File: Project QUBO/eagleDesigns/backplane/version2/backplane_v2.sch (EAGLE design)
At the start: 5 parts

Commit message: 
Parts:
- added G10, G4, G5, G6, G7, G8, G9: (no value), avx:F930J107MBA
- added G2, G3: (no value), texas:TPS2044BBD-SOIC
- added U1: TUSB2077ALQFP, texas:TUSB2077ALQFP
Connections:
- new net !OVERCUR1!: G2.!OC1!
- new net !OVERCUR2!: G2.!OC2!
- new net !OVERCUR3!: G2.!OC3!
- new net !OVERCUR4!: G2.!OC4!
- new net !OVERCUR5!: G3.!OC1!
- new net !OVERCUR6!: G3.!OC2!
- new net !OVERCUR7!: G3.!OC3!
- new net !PWRON1!: G2.!EN1!
- new net !PWRON2!: G2.!EN2!
- new net !PWRON3!: G2.!EN3!
- new net !PWRON4!: G2.!EN4!
- new net !PWRON5!: G3.!EN1!
- new net !PWRON6!: G3.!EN2!
- new net !PWRON7!: G3.!EN3!
- new net N$1: U1.SUSPND
- new net N$11: U1.!PWRON1!
- new net N$12: U1.!OVERCUR1!
- new net N$13: U1.DM1
- new net N$14: U1.DP1
- new net N$15: U1.!PWRON2!
- new net N$16: U1.!OVERCUR2!
- new net N$17: U1.DM2
- new net N$18: U1.DP2
- new net N$19: U1.!PWRON3!
- new net N$2: U1.DP0PUR
- new net N$20: U1.!OVERCUR3!
- new net N$21: U1.DM3
- new net N$22: U1.DP3
- new net N$23: U1.!PWRON4!
- new net N$25: U1.!OVERCUR4!
- new net N$26: U1.DM4
- new net N$27: U1.DP4
- new net N$28: U1.!PWRON5!
- new net N$29: U1.!OVERCUR5!
- new net N$3: U1.DP0
- new net N$30: U1.DM5
- new net N$31: U1.DP5
- new net N$32: U1.!PWRON6!
- new net N$33: U1.!OVERCUR6!
- new net N$34: U1.DM6
- new net N$35: U1.DP6
- new net N$36: U1.!PWRON7!
- new net N$4: U1.DM0
- new net N$40: U1.XTAL1/CLK48
- new net N$41: U1.XTAL2
- new net N$43: U1.PORTDIS
- new net N$44: U1.PORTPWR
- new net N$45: U1.HUBCFG
- new net N$46: U1.DP7
- new net N$47: U1.DM7
- new net N$48: U1.!OVERCUR7!
- new net N$7: U1.EECLK
- new net USB-5V_2: G2.OUT2, JP2.P$63
- new net USB-5V_3: G2.OUT3, JP3.P$63
- new net USB-5V_4: G2.OUT4, JP4.P$63
- new net USB-5V_5: G3.OUT1
- new net USB-5V_6: G3.OUT2
- new net USB-5V_7: G3.OUT3
- net 3V3: now also U1.!BUSPWR!, U1.!EXTMEM!, U1.EEDATA/!GANGED!, U1.VCC@46, U1.VCC@9
- net 5V: now also G2.IN1, G2.IN2, G3.IN1, G3.IN2
- net GND: now also G2.GND1, G2.GND2, G3.GND1, G3.GND2, U1.GND@24, U1.GND@43, U1.GND@5, U1.MODE
- net GPIO_3: now also U1.!RESET!
- net USB-5V_1: now also G2.OUT1; no longer JP2.P$63, JP3.P$63, JP4.P$63

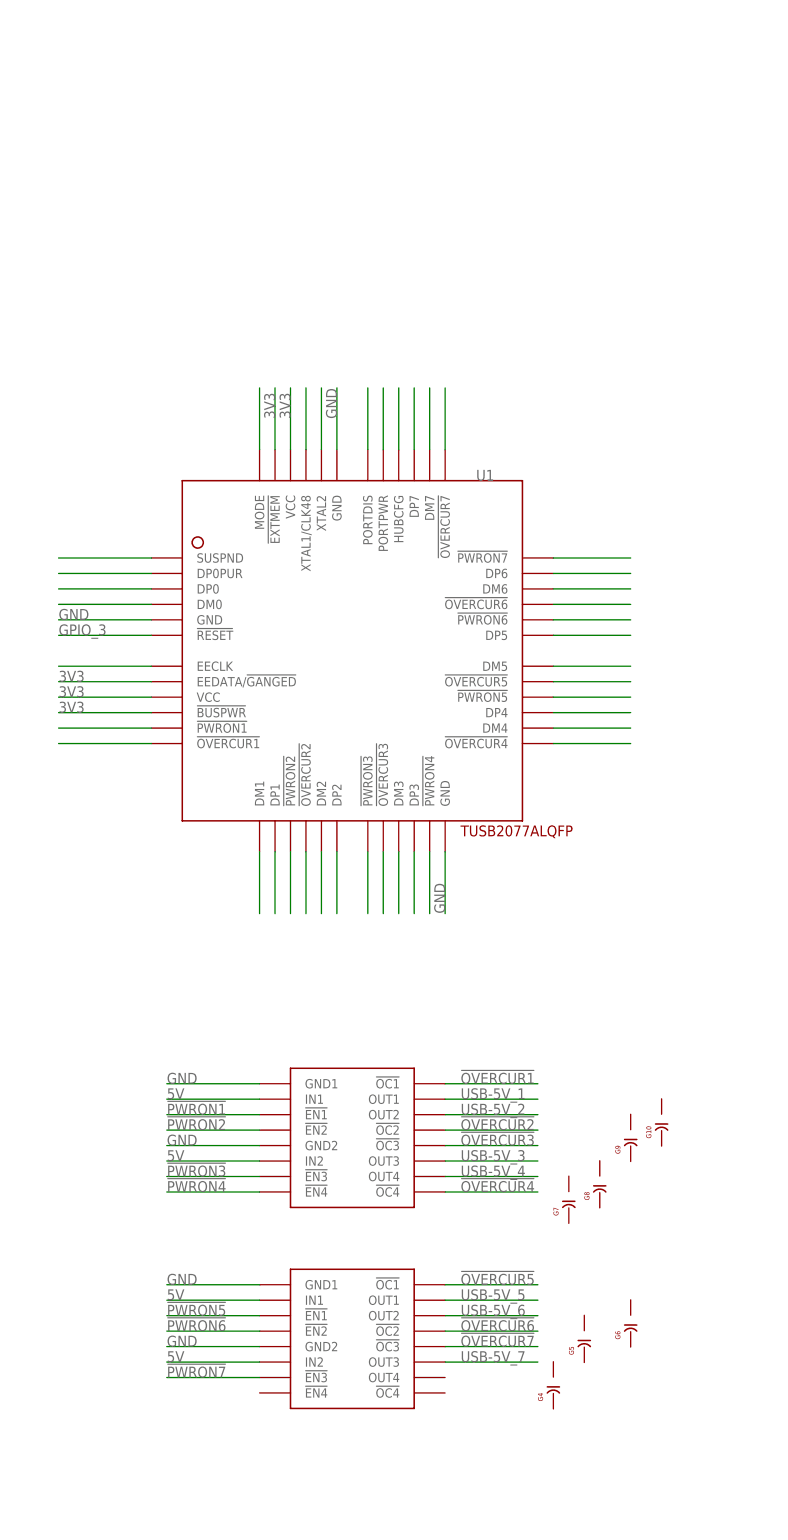
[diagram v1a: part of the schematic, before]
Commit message: 
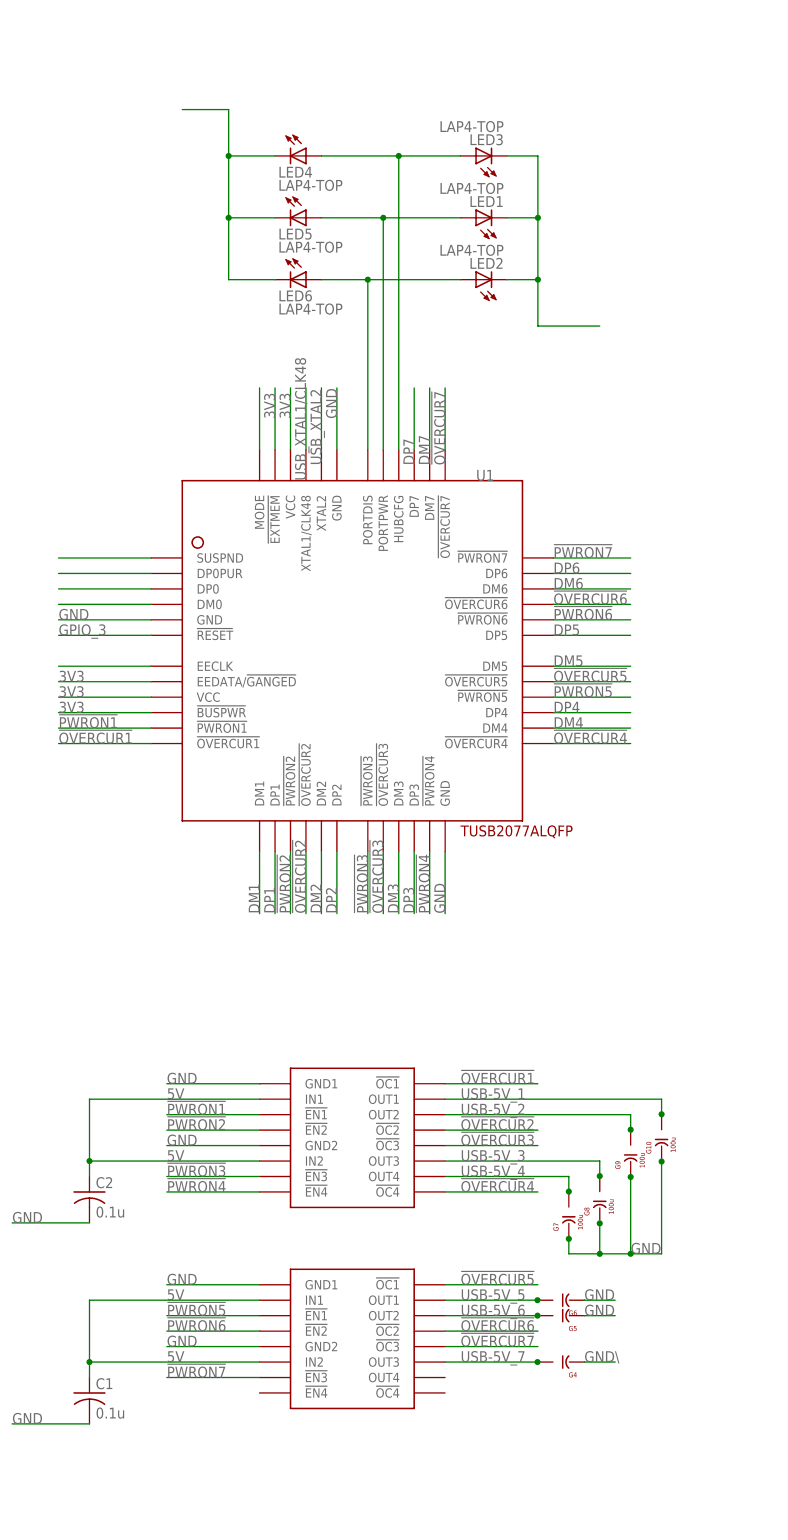
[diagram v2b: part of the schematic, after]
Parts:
- added C1, C2: 0.1u, resistor:C-USC0603
- added LED1, LED2, LED3, LED4, LED5, LED6: LAP4-TOP, led:LAP4-TOP
- G10, G7, G8, G9: value (none) -> 100u
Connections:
- net N$13 renamed DM1
- net N$14 renamed DP1
- net N$17 renamed DM2
- net N$18 renamed DP2
- net N$21 renamed DM3
- net N$22 renamed DP3
- net N$26 renamed DM4
- net N$27 renamed DP4
- net N$30 renamed DM5
- net N$31 renamed DP5
- net N$34 renamed DM6
- net N$35 renamed DP6
- net N$40 renamed USB_XTAL1/CLK48
- net N$41 renamed USB_XTAL2
- net N$46 renamed DP7
- net N$47 renamed DM7
- removed net N$11: U1.!PWRON1!
- removed net N$12: U1.!OVERCUR1!
- removed net N$15: U1.!PWRON2!
- removed net N$16: U1.!OVERCUR2!
- removed net N$19: U1.!PWRON3!
- removed net N$20: U1.!OVERCUR3!
- removed net N$23: U1.!PWRON4!
- removed net N$25: U1.!OVERCUR4!
- removed net N$28: U1.!PWRON5!
- removed net N$29: U1.!OVERCUR5!
- removed net N$32: U1.!PWRON6!
- removed net N$33: U1.!OVERCUR6!
- removed net N$36: U1.!PWRON7!
- removed net N$48: U1.!OVERCUR7!
- new net N$5: LED4.C, LED5.C, LED6.C
- net !OVERCUR1!: now also U1.!OVERCUR1!
- net !OVERCUR2!: now also U1.!OVERCUR2!
- net !OVERCUR3!: now also U1.!OVERCUR3!
- net !OVERCUR4!: now also U1.!OVERCUR4!
- net !OVERCUR5!: now also U1.!OVERCUR5!
- net !OVERCUR6!: now also U1.!OVERCUR6!
- net !OVERCUR7!: now also U1.!OVERCUR7!
- net !PWRON1!: now also U1.!PWRON1!
- net !PWRON2!: now also U1.!PWRON2!
- net !PWRON3!: now also U1.!PWRON3!
- net !PWRON4!: now also U1.!PWRON4!
- net !PWRON5!: now also U1.!PWRON5!
- net !PWRON6!: now also U1.!PWRON6!
- net !PWRON7!: now also U1.!PWRON7!
- net 5V: now also C1.1, C2.1
- net GND: now also C1.2, C2.2, G10.-, G7.-, G8.-, G9.-, LED1.C, LED2.C, LED3.C
- net N$43: now also LED2.A, LED6.A
- net N$44: now also LED1.A, LED5.A
- net N$45: now also LED3.A, LED4.A
- net USB-5V_1: now also G10.+
- net USB-5V_2: now also G9.+
- net USB-5V_3: now also G8.+
- net USB-5V_4: now also G7.+
- net USB-5V_5: now also G6.+
- net USB-5V_6: now also G5.+
- net USB-5V_7: now also G4.+
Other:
- moved on the sheet: G10, G4, G5, G6, G7, G8, G9

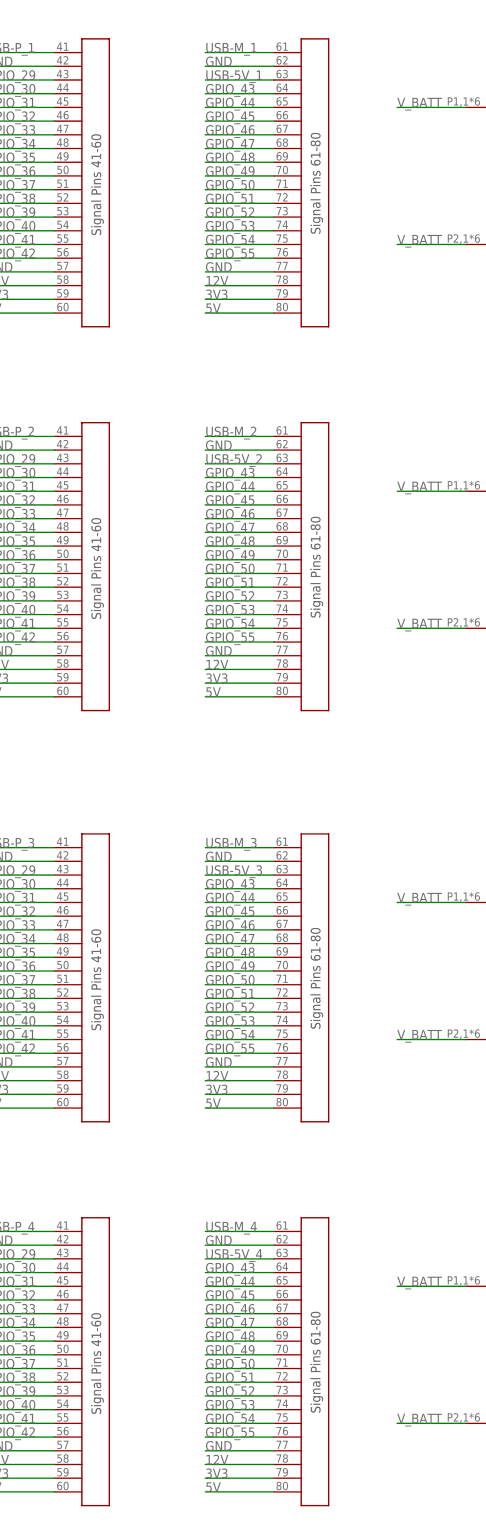
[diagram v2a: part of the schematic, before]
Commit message: 
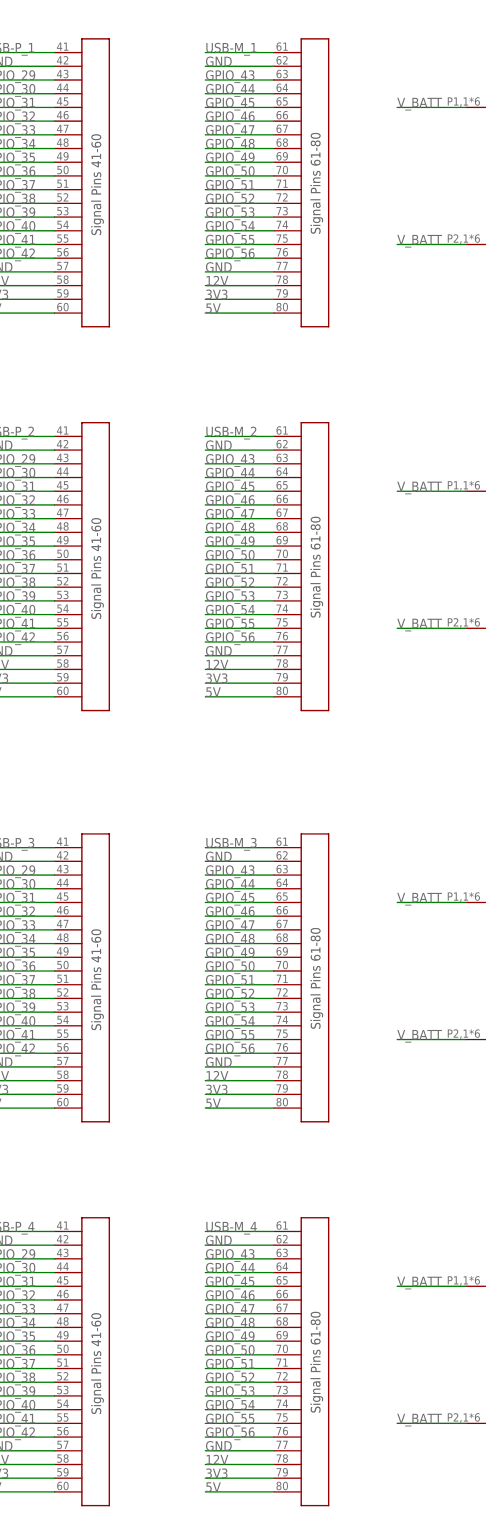
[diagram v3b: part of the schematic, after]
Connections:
- new net GPIO_56: JP1.P$76, JP2.P$76, JP3.P$76, JP4.P$76
- net GPIO_43: now also JP1.P$63, JP2.P$63, JP3.P$63, JP4.P$63; no longer JP1.P$64, JP2.P$64, JP3.P$64, JP4.P$64
- net GPIO_44: now also JP1.P$64, JP2.P$64, JP3.P$64, JP4.P$64; no longer JP1.P$65, JP2.P$65, JP3.P$65, JP4.P$65
- net GPIO_45: now also JP1.P$65, JP2.P$65, JP3.P$65, JP4.P$65; no longer JP1.P$66, JP2.P$66, JP3.P$66, JP4.P$66
- net GPIO_46: now also JP1.P$66, JP2.P$66, JP3.P$66, JP4.P$66; no longer JP1.P$67, JP2.P$67, JP3.P$67, JP4.P$67
- net GPIO_47: now also JP1.P$67, JP2.P$67, JP3.P$67, JP4.P$67; no longer JP1.P$68, JP2.P$68, JP3.P$68, JP4.P$68
- net GPIO_48: now also JP1.P$68, JP2.P$68, JP3.P$68, JP4.P$68; no longer JP1.P$69, JP2.P$69, JP3.P$69, JP4.P$69
- net GPIO_49: now also JP1.P$69, JP2.P$69, JP3.P$69, JP4.P$69; no longer JP1.P$70, JP2.P$70, JP3.P$70, JP4.P$70
- net GPIO_50: now also JP1.P$70, JP2.P$70, JP3.P$70, JP4.P$70; no longer JP1.P$71, JP2.P$71, JP3.P$71, JP4.P$71
- net GPIO_51: now also JP1.P$71, JP2.P$71, JP3.P$71, JP4.P$71; no longer JP1.P$72, JP2.P$72, JP3.P$72, JP4.P$72
- net GPIO_52: now also JP1.P$72, JP2.P$72, JP3.P$72, JP4.P$72; no longer JP1.P$73, JP2.P$73, JP3.P$73, JP4.P$73
- net GPIO_53: now also JP1.P$73, JP2.P$73, JP3.P$73, JP4.P$73; no longer JP1.P$74, JP2.P$74, JP3.P$74, JP4.P$74
- net GPIO_54: now also JP1.P$74, JP2.P$74, JP3.P$74, JP4.P$74; no longer JP1.P$75, JP2.P$75, JP3.P$75, JP4.P$75
- net GPIO_55: now also JP1.P$75, JP2.P$75, JP3.P$75, JP4.P$75; no longer JP1.P$76, JP2.P$76, JP3.P$76, JP4.P$76
- net USB-5V_1: no longer JP1.P$63
- net USB-5V_2: no longer JP2.P$63
- net USB-5V_3: no longer JP3.P$63
- net USB-5V_4: no longer JP4.P$63
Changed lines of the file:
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@@
 </segment>
 </net>
-<net name="GPIO_55" class="0">
+<net name="GPIO_56" class="0">
 <segment>
 <pinref part="JP1" gate="G$1" pin="P$76"/>
@@
 </segment>
 </net>
-<net name="GPIO_54" class="0">
+<net name="GPIO_55" class="0">
 <segment>
 <pinref part="JP1" gate="G$1" pin="P$75"/>
@@
 </segment>
 </net>
-<net name="GPIO_53" class="0">
+<net name="GPIO_54" class="0">
 <segment>
 <pinref part="JP1" gate="G$1" pin="P$74"/>
@@
 </segment>
 </net>
-<net name="GPIO_52" class="0">
+<net name="GPIO_53" class="0">
 <segment>
 <pinref part="JP1" gate="G$1" pin="P$73"/>
@@
 </segment>
 </net>
-<net name="GPIO_51" class="0">
+<net name="GPIO_52" class="0">
 <segment>
 <pinref part="JP1" gate="G$1" pin="P$72"/>
@@
 </segment>
 </net>
-<net name="GPIO_50" class="0">
+<net name="GPIO_51" class="0">
 <segment>
 <pinref part="JP1" gate="G$1" pin="P$71"/>
@@
 </segment>
 </net>
-<net name="GPIO_49" class="0">
+<net name="GPIO_50" class="0">
 <segment>
 <pinref part="JP1" gate="G$1" pin="P$70"/>
@@
 </segment>
 </net>
-<net name="GPIO_48" class="0">
+<net name="GPIO_49" class="0">
 <segment>
 <pinref part="JP1" gate="G$1" pin="P$69"/>
@@
 </segment>
 </net>
-<net name="GPIO_47" class="0">
+<net name="GPIO_48" class="0">
 <segment>
 <pinref part="JP1" gate="G$1" pin="P$68"/>
@@
 </segment>
 </net>
-<net name="GPIO_46" class="0">
+<net name="GPIO_47" class="0">
 <segment>
 <pinref part="JP1" gate="G$1" pin="P$67"/>
@@
 </segment>
 </net>
-<net name="GPIO_45" class="0">
+<net name="GPIO_46" class="0">
 <segment>
 <pinref part="JP1" gate="G$1" pin="P$66"/>
@@
 </segment>
 </net>
-<net name="GPIO_44" class="0">
+<net name="GPIO_45" class="0">
 <segment>
 <pinref part="JP1" gate="G$1" pin="P$65"/>
@@
 </segment>
 </net>
-<net name="GPIO_43" class="0">
+<net name="GPIO_44" class="0">
 <segment>
 <pinref part="JP1" gate="G$1" pin="P$64"/>
@@
 </net>
 <net name="USB-5V_1" class="0">
-<segment>
-<pinref part="JP1" gate="G$1" pin="P$63"/>
-<wire x1="109.22" y1="91.44" x2="96.52" y2="91.44" width="0.1524" layer="91"/>
-<label x="96.52" y="91.44" size="1.778" layer="95"/>
-</segment>
 <segment>
 <pinref part="G2" gate="G$1" pin="OUT1"/>
@@
 <junction x="-193.04" y="-88.836"/>
 </segment>
-<segment>
-<pinref part="JP2" gate="G$1" pin="P$63"/>
-<wire x1="109.22" y1="20.32" x2="96.52" y2="20.32" width="0.1524" layer="91"/>
-<label x="96.52" y="20.32" size="1.778" layer="95"/>
-</segment>
 </net>
 <net name="!OVERCUR2!" class="0">
@@
 </net>
 <net name="USB-5V_3" class="0">
-<segment>
-<pinref part="JP3" gate="G$1" pin="P$63"/>
-<wire x1="109.22" y1="-55.88" x2="96.52" y2="-55.88" width="0.1524" layer="91"/>
-<label x="96.52" y="-55.88" size="1.778" layer="95"/>
-</segment>
 <segment>
 <pinref part="G2" gate="G$1" pin="OUT3"/>
@@
 </net>
 <net name="USB-5V_4" class="0">
-<segment>
-<pinref part="JP4" gate="G$1" pin="P$63"/>
-<wire x1="109.22" y1="-127" x2="96.52" y2="-127" width="0.1524" layer="91"/>
-<label x="96.52" y="-127" size="1.778" layer="95"/>
-</segment>
 <segment>
 <pinref part="G2" gate="G$1" pin="OUT4"/>
@@
 </segment>
 </net>
+<net name="GPIO_43" class="0">
+<segment>
+<pinref part="JP1" gate="G$1" pin="P$63"/>
+<wire x1="109.22" y1="91.44" x2="96.52" y2="91.44" width="0.1524" layer="91"/>
+<label x="96.52" y="91.44" size="1.778" layer="95"/>
+</segment>
+<segment>
+<pinref part="JP2" gate="G$1" pin="P$63"/>
+<wire x1="109.22" y1="20.32" x2="96.52" y2="20.32" width="0.1524" layer="91"/>
+<label x="96.52" y="20.32" size="1.778" layer="95"/>
+</segment>
+<segment>
+<pinref part="JP3" gate="G$1" pin="P$63"/>
+<wire x1="109.22" y1="-55.88" x2="96.52" y2="-55.88" width="0.1524" layer="91"/>
+<label x="96.52" y="-55.88" size="1.778" layer="95"/>
+</segment>
+<segment>
+<pinref part="JP4" gate="G$1" pin="P$63"/>
+<wire x1="109.22" y1="-127" x2="96.52" y2="-127" width="0.1524" layer="91"/>
+<label x="96.52" y="-127" size="1.778" layer="95"/>
+</segment>
+</net>
